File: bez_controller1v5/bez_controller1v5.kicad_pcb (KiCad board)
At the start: 4 copper layers, 75 parts, among them J1 Conn_01x03_Male, J10 IMU Conn_01x03_Female, J11 Conn_01x03_Male, J12 Conn_01x03_Male, J13 USB_B_Mini, J2 Conn_01x03_Male, J3 Conn_01x03_Male, J4 Screw_Terminal_01x02, J5 Conn_01x03_Male, J6 Conn_01x03_Male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

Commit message: new route PCB
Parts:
- moved D4 9.67 mm to (34.4, 40.2), turned to 0 degrees
- moved C15 8.51 mm to (37.9, 51.7), turned to 180 degrees
- moved J10 8.18 mm to (89.0, 79.6)
- moved C6 6.99 mm to (37.9, 49.7), turned to 180 degrees
- moved C16 5.24 mm to (52.3, 46.9), turned to 90 degrees
- moved J9 1.66 mm to (82.6, 61.8)
- moved R6 1.32 mm to (38.9, 64.4), turned to 90 degrees
- moved J1 1.31 mm to (40.8, 76.6)
- moved U10 0.72 mm to (45.0, 40.1)
- moved J4 0.68 mm to (78.1, 32.2)
- moved J13 0.56 mm to (45.2, 28.3)
- moved FB1 0.15 mm to (62.5, 61.7)
- turned R10 to -90 degrees
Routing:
- net GND: track 179.9 -> 194.4 mm, vias 23 -> 17
- net Net-(D4-A): track 19.2 -> 7.40 mm
- net /I2C_SDA: track 104.9 -> 95.0 mm
- net /I2C_SCL: track 105.7 -> 95.9 mm
- net /MOTOR_DATA2: track 27.0 -> 18.6 mm
- net Net-(U7-VCAP_1): track 12.4 -> 5.48 mm
- net +3.3V: track 76.9 -> 70.9 mm, vias 9 -> 8
- net /USART5_DIR: track 112.2 -> 106.4 mm
- net /MOTOR_DATA1: track 25.9 -> 20.4 mm
- net /MOTOR_DATA5: track 33.3 -> 28.8 mm
- net /MOTOR_DATA4: track 33.1 -> 28.9 mm
- net /MOTOR_DATA3: track 29.6 -> 25.4 mm
- net +5V: track 83.5 -> 87.1 mm
- net /BOOT0: track 12.8 -> 9.66 mm
- net /USART6_RX: track 126.7 -> 124.0 mm
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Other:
- board outline added: 98 x 57.6 mm

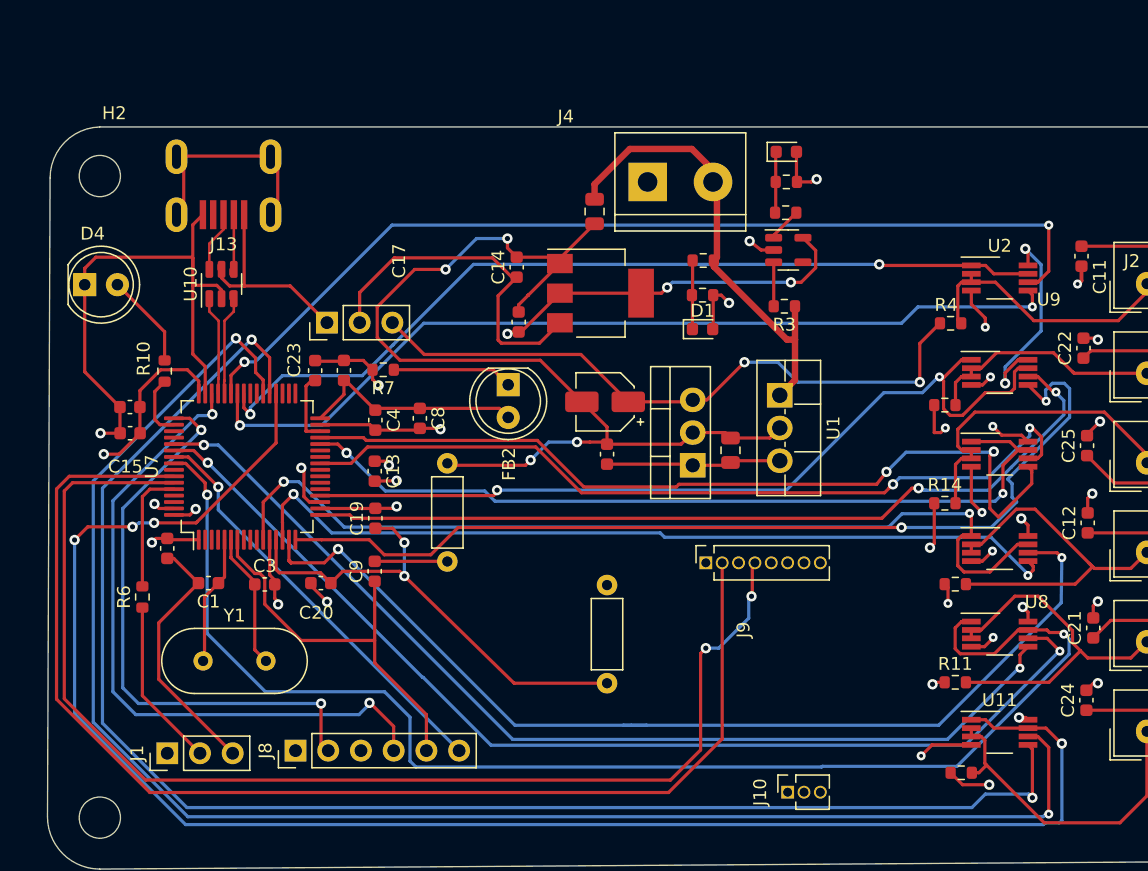
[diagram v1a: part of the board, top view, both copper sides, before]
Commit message: Added connection for Voltage Measurement and Current Measurement, also cleaned up PCB a little more
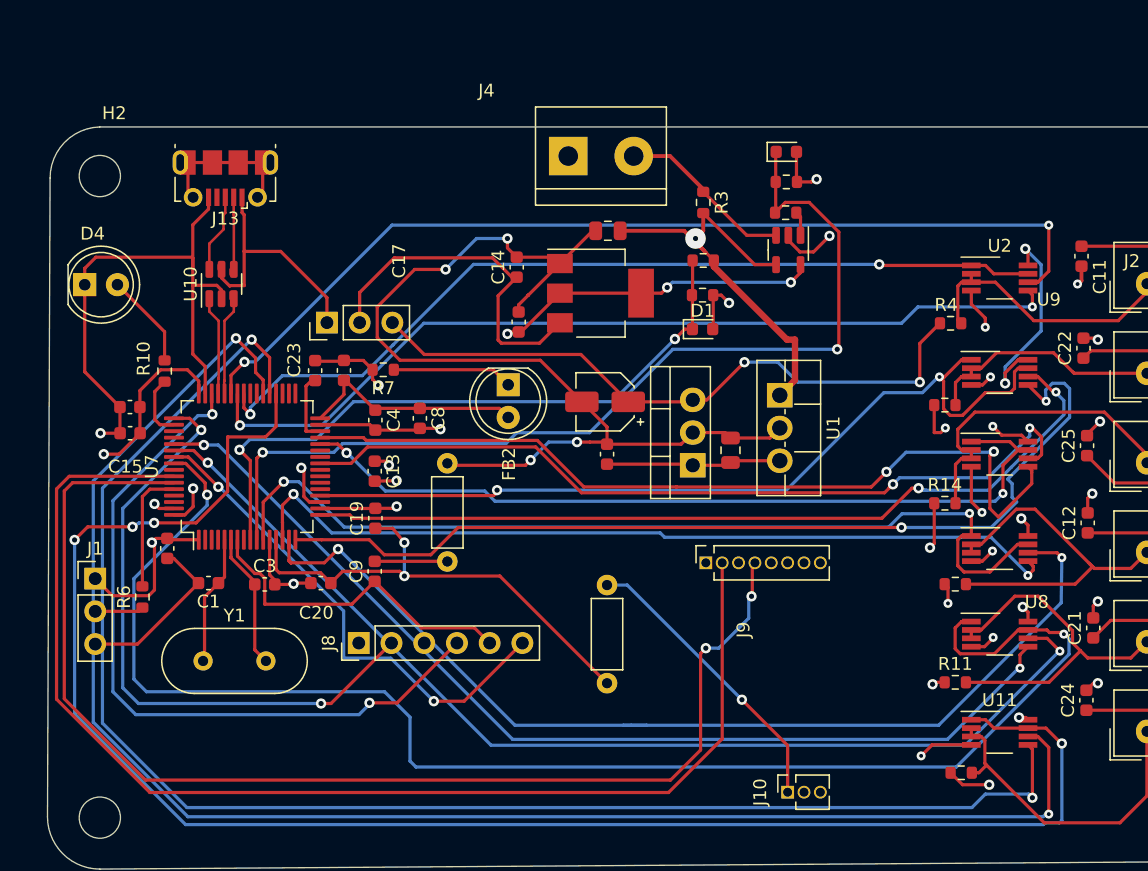
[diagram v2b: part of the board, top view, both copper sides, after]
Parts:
- J13: footprint USB:USB_Micro-B_Molex-105017-0001 -> Connector_USB:USB_Micro-B_Molex-105017-0001
- moved J1 14.7 mm to (35.2, 63.0), turned to 0 degrees
- moved R3 10.2 mm to (82.4, 33.8), turned to -90 degrees
- moved J8 9.69 mm to (55.7, 68.0)
- moved J4 6.48 mm to (71.9, 30.2)
- moved J13 3.69 mm to (45.3, 31.9)
- moved C2 1.82 mm to (75.0, 36.0), turned to 180 degrees
- turned U6 to -90 degrees
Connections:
- J10 pad 1: /VDD -> +3.3V
- R3 pad 2: Net-(U6-+) -> +12V
- U6 pad 3: Net-(U6-+) -> +12V
- U6 pad 4: Net-(U6--) -> +12V
- U7 pad 10: /Button -> /V_shunt_read
- U7 pad 9: /Reset Button -> /V_bat_read
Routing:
- net /V_shunt_read: track 4.76 -> 75.0 mm, vias 0 -> 2
- net /V_bat_read: track 5.37 -> 51.7 mm, vias 0 -> 2
- net +3.3V: track 70.9 -> 100.7 mm, vias 8 -> 9
- net +12V: track 44.5 -> 55.3 mm, vias 6 -> 7
- net /USART5_DIR: track 106.4 -> 116.5 mm
- net Net-(J1-Pin_2): track 13.2 -> 3.78 mm
- net /SWO: track 32.6 -> 39.2 mm, vias 1 -> 2
- net unconnected-(J13-Shield-Pad6): track 16.3 -> 11.5 mm
- net /NRST: track 30.6 -> 26.3 mm
- net GND: track 194.4 -> 190.3 mm, vias 17 -> 16
- net /TMS: track 52.8 -> 56.8 mm
- net VBUS: track 16.2 -> 19.8 mm
- net /TCK: track 44.9 -> 48.4 mm
- net Net-(U6-+): track 3.42 -> 0.00 mm
- net /USART6_DIR: track 130.7 -> 132.4 mm
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
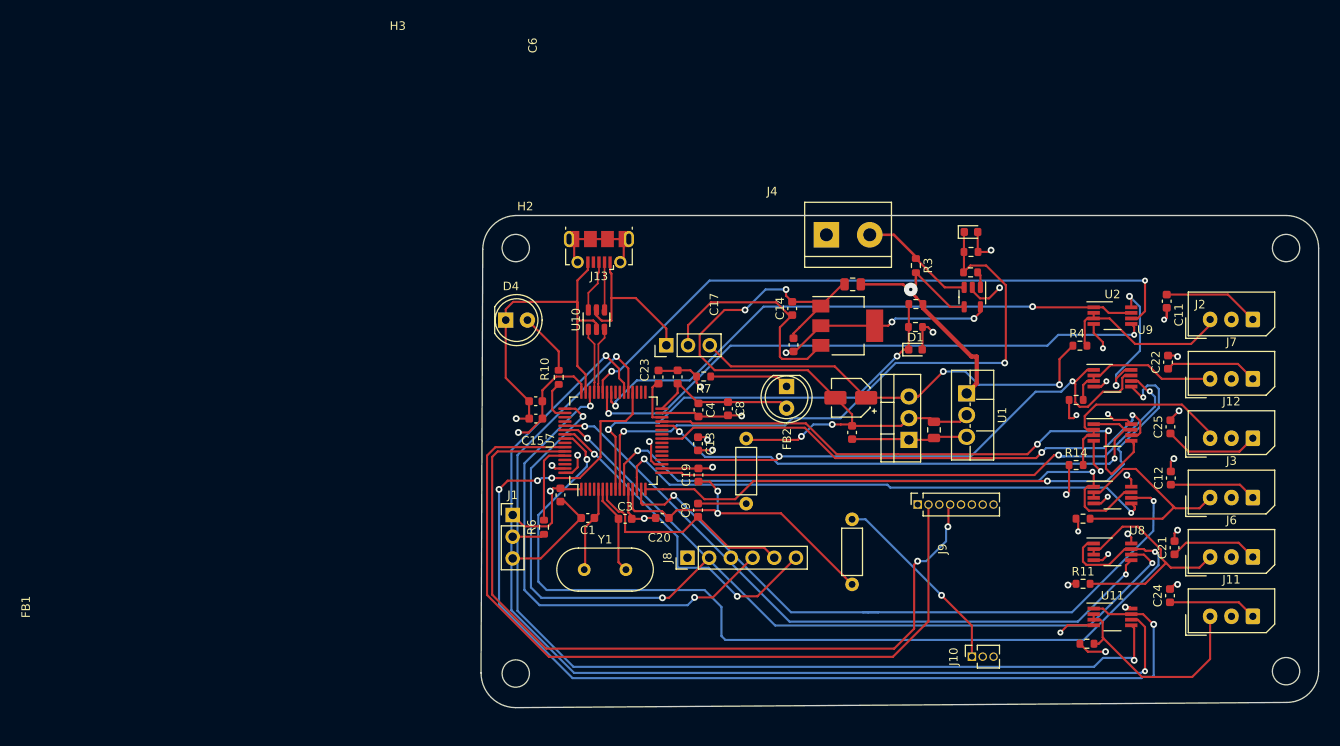
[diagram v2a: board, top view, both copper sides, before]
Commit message: fixing some routing and components footprint
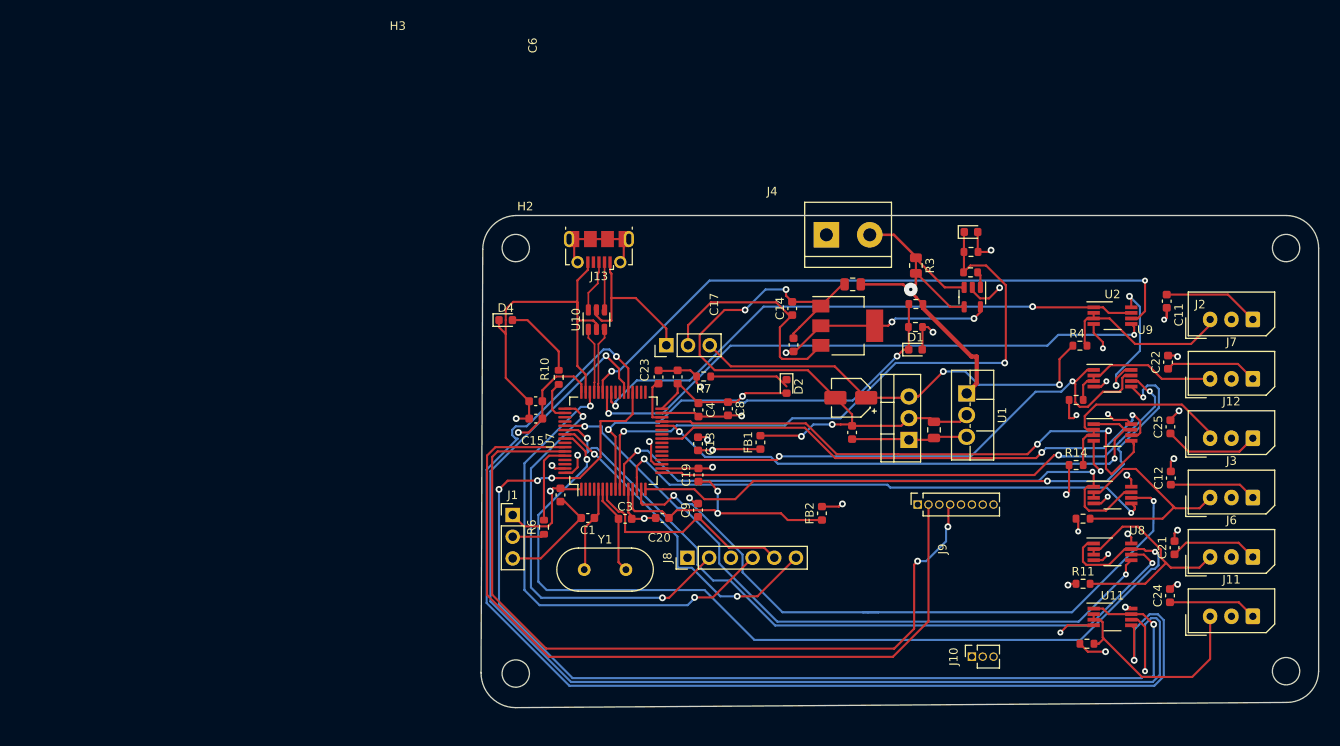
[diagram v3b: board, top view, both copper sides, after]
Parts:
- D2, D4: footprint LED_THT:LED_D5.0mm_Clear -> LED_SMD:LED_0603_1608Metric
- FB1, FB2: footprint Inductor_THT:L_Axial_L5.3mm_D2.2mm_P7.62mm_Horizontal_Vishay_IM-1 -> Inductor_SMD:L_0603_1608Metric
- R3: footprint Resistor_SMD:R_0603_1608Metric -> Resistor_SMD:R_0805_2012Metric
- moved FB2 9.04 mm to (71.4, 62.8)
- moved FB1 7.36 mm to (64.2, 54.5)
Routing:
- net /USART6_TX: track 119.1 -> 146.0 mm
- net +3.3V: track 100.7 -> 80.7 mm, vias 9 -> 10
- net /USART6_RX: track 124.0 -> 143.2 mm
- net +3.3VA: track 38.0 -> 31.3 mm
- net GND: track 190.3 -> 193.0 mm, vias 16 -> 17
- net /USART5_RX: track 84.4 -> 86.9 mm
- net /USART5_DIR: track 116.5 -> 114.5 mm
- net /PWR_GND: track 79.3 -> 77.5 mm
- net Net-(D4-A): track 7.40 -> 9.15 mm
- net /USART5_TX: track 79.9 -> 81.6 mm
- net +12V: track 55.3 -> 57.0 mm
- net /USART4_RX: track 80.3 -> 81.5 mm

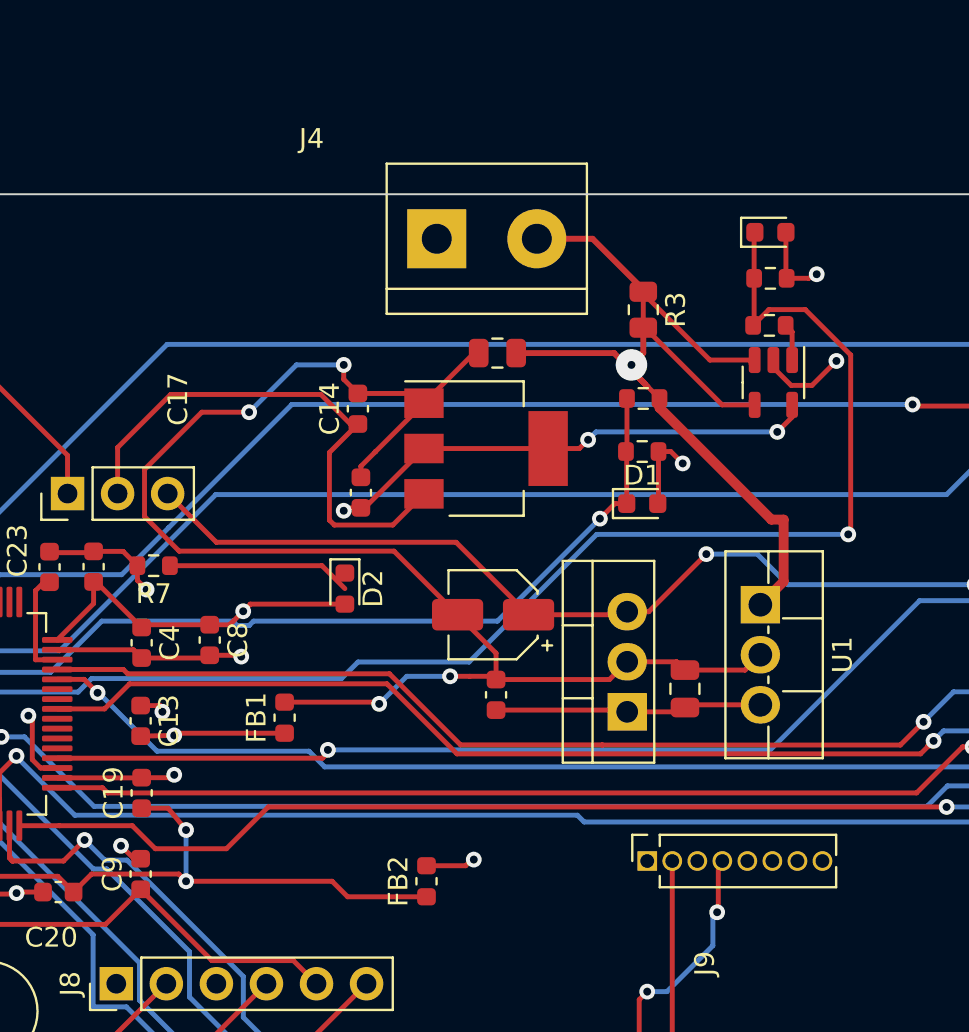
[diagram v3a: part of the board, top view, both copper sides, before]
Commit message: change footprint of shunt R and electrolytic C
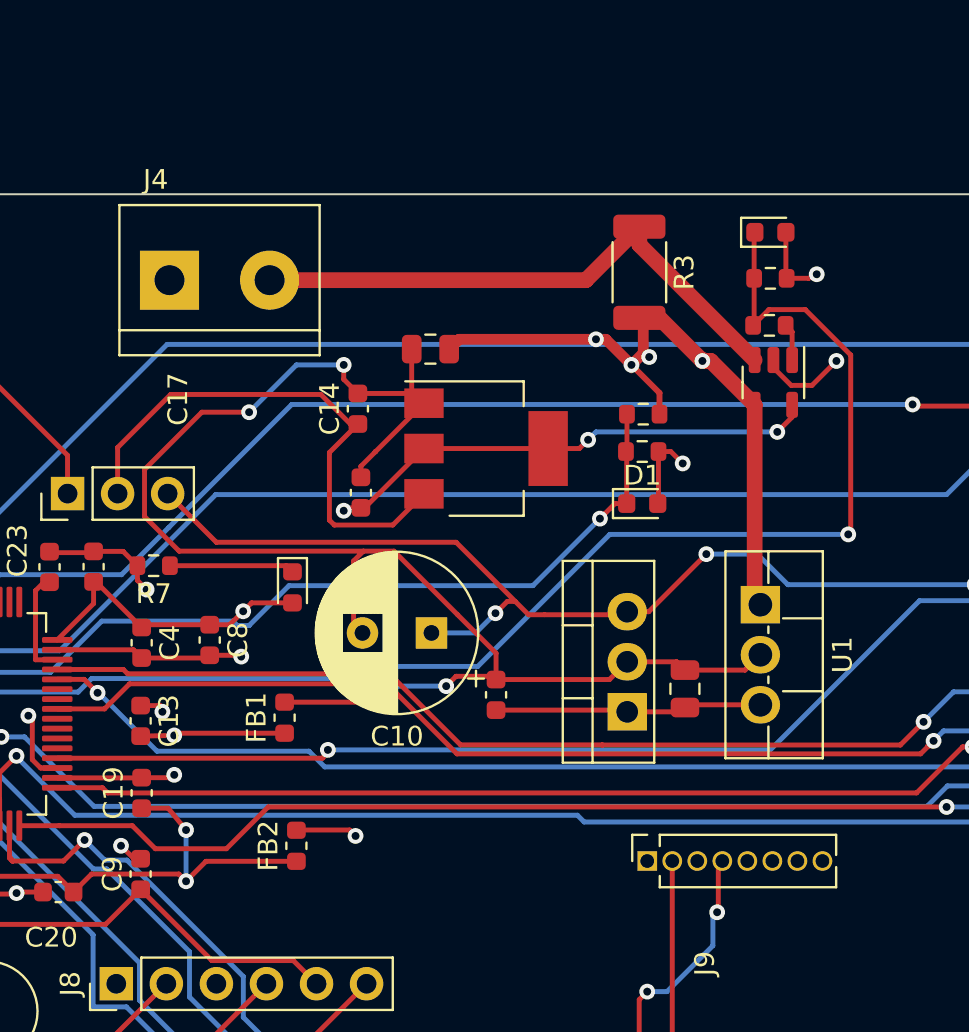
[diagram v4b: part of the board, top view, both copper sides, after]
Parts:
- C10: footprint Capacitor_SMD:CP_Elec_4x5.4 -> Capacitor_THT:CP_Radial_D8.0mm_P3.50mm
- R3: footprint Resistor_SMD:R_0805_2012Metric -> Resistor_SMD:R_2010_5025Metric
- moved J4 13.7 mm to (58.4, 32.3)
- moved FB2 6.84 mm to (64.8, 61.0)
- moved C2 3.41 mm to (71.6, 35.8)
- moved C10 3.26 mm to (71.7, 50.2)
- moved D2 2.66 mm to (64.6, 47.9)
- moved R3 1.91 mm to (82.2, 31.9)
- moved R1 0.80 mm to (82.4, 39.1)
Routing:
- net +12V: track 57.0 -> 71.3 mm, vias 7 -> 10
- net +3.3VA: track 31.3 -> 24.8 mm
- net +5V: track 87.1 -> 92.0 mm, vias 13 -> 14
- net /PWR_GND: track 77.5 -> 81.3 mm
- net Net-(D2-K): track 9.36 -> 6.35 mm
- net +3.3V: track 80.7 -> 78.3 mm
- net /V_bat_read: track 51.9 -> 51.1 mm

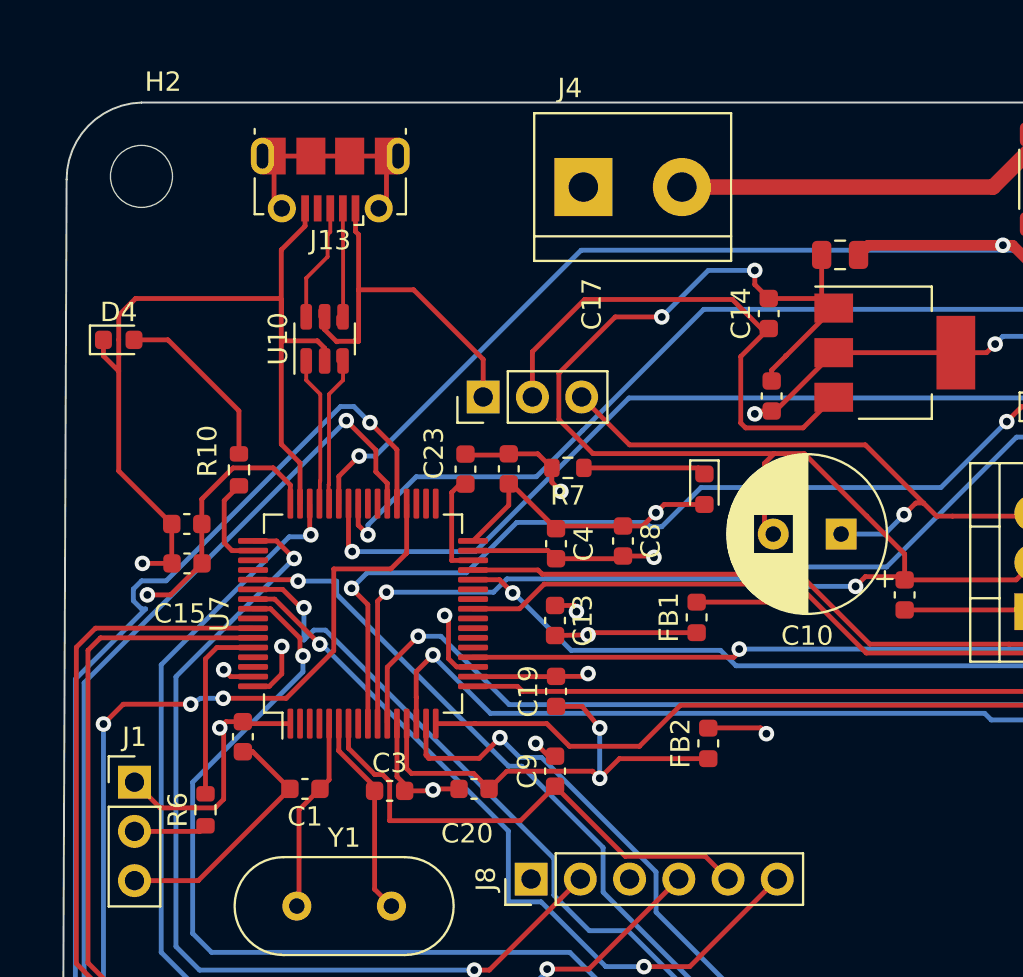
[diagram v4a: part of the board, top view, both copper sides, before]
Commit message: added USB footprint
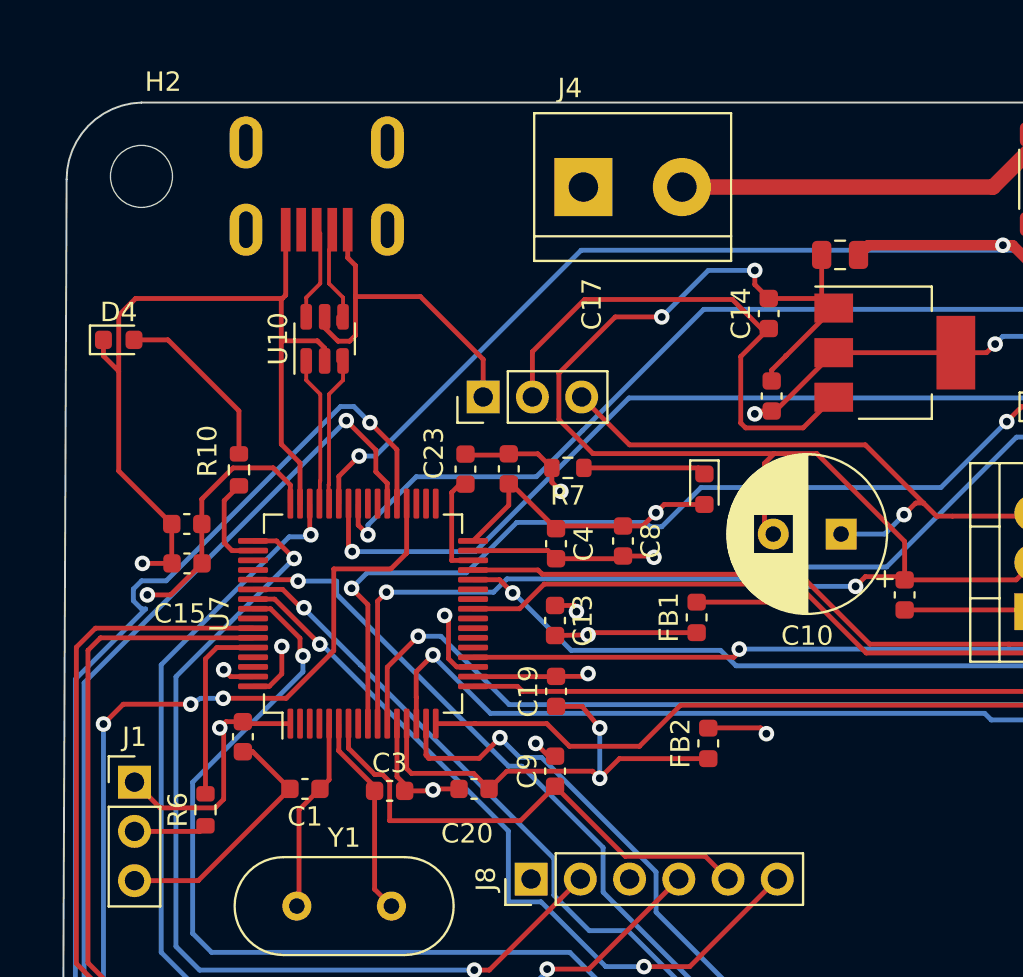
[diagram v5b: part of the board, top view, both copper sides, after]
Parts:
- J13: footprint Connector_USB:USB_Micro-B_Molex-105017-0001 -> USB-Library:USB_MINI
- R3: value 40m -> 5m
- moved J13 0.70 mm to (44.6, 31.9)
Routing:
- net unconnected-(J13-Shield-Pad6): track 11.5 -> 0.00 mm
- net GND: track 193.0 -> 190.6 mm
- net VBUS: track 19.8 -> 18.1 mm
- net /USART5_RX: track 86.9 -> 85.6 mm
- net /USB_CONN_D+: track 6.11 -> 4.87 mm
- net /USB_CONN_D-: track 5.98 -> 5.25 mm
